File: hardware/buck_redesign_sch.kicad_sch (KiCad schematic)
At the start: 25 parts, among them Q7 MMBT3904, U101 L7987L, U5 TLV1701

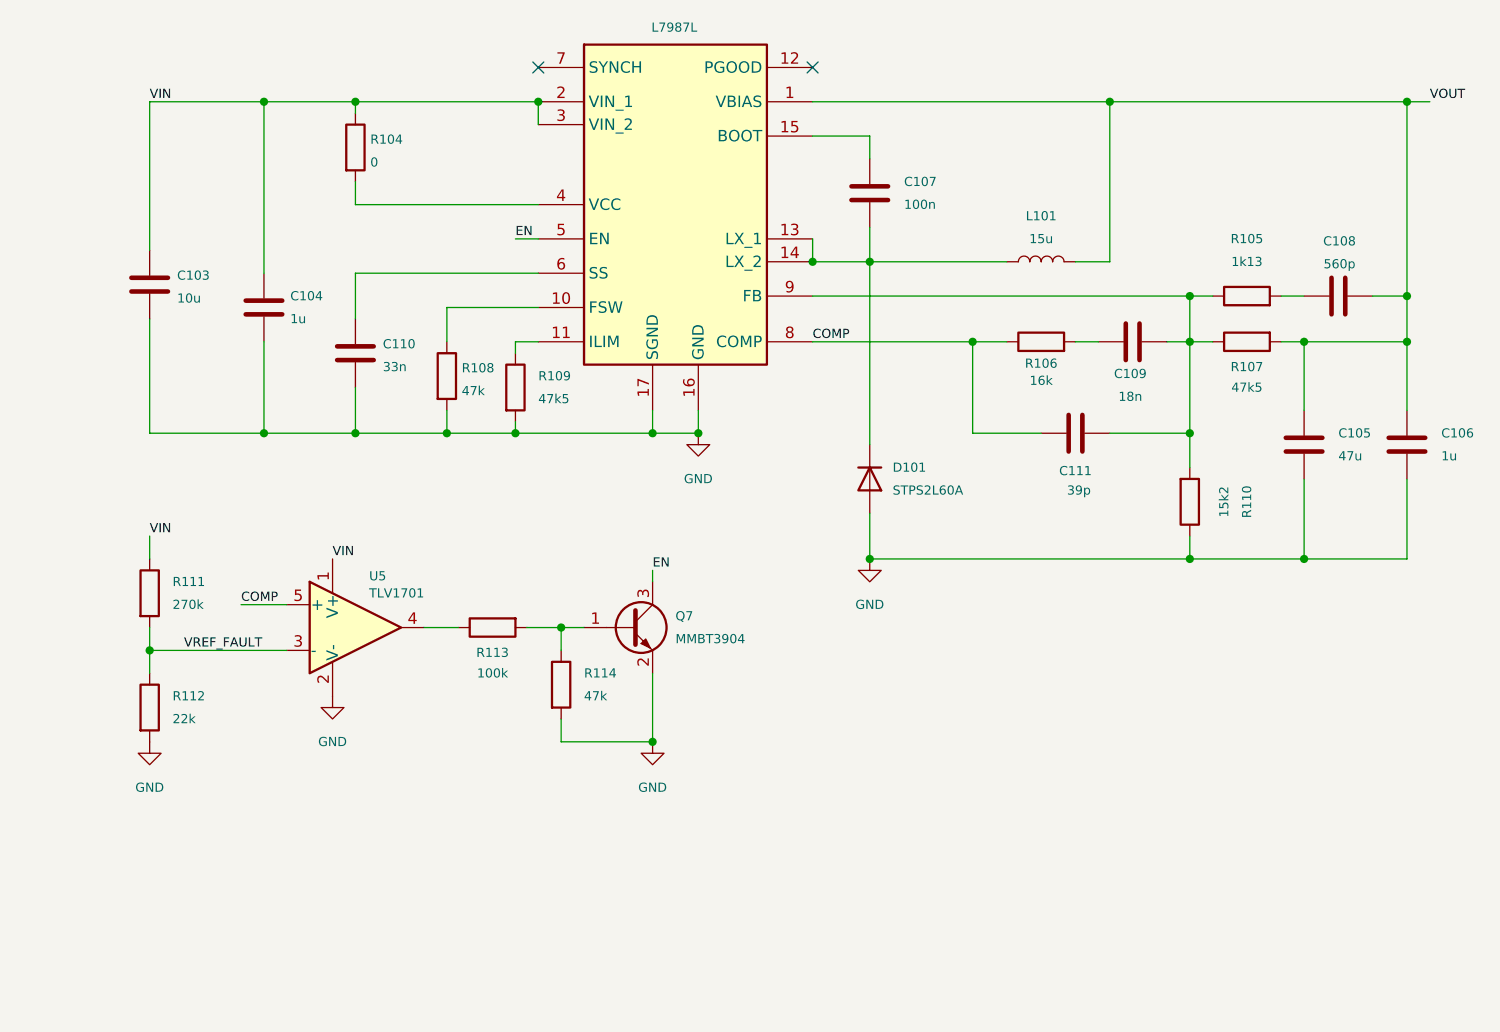
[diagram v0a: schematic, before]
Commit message: Corrected pins in TLV1701 symbol and added bypass cap on its V+
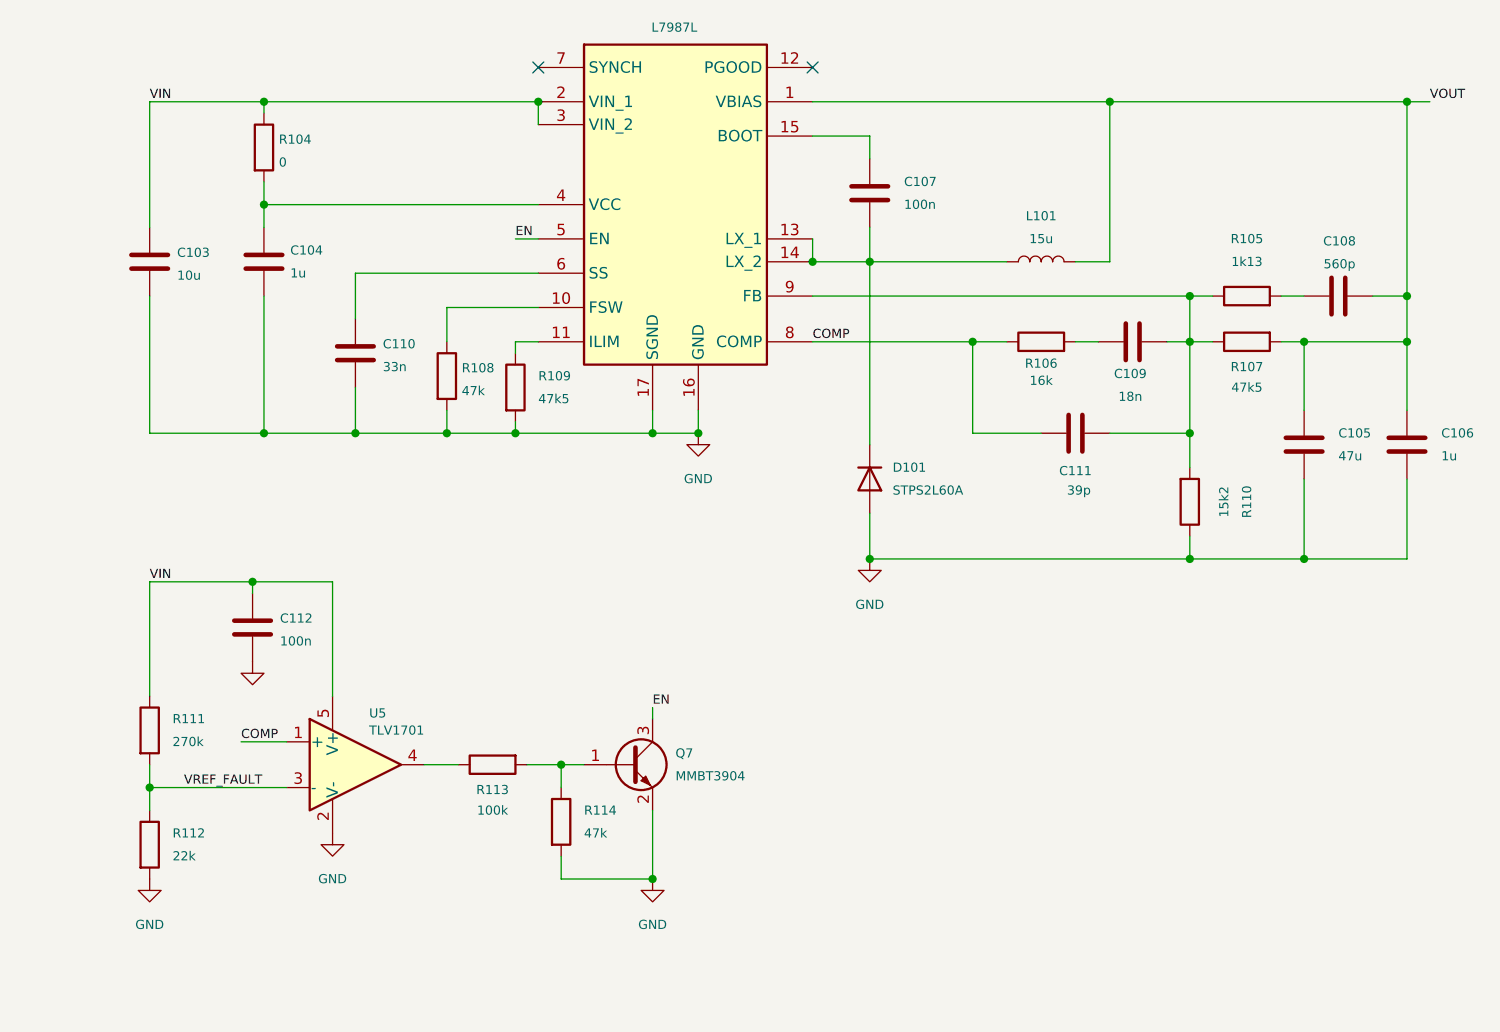
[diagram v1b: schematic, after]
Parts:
- added C112: 100n, symbol Device:C
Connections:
- net COMP: now also U5.1 (+); no longer U5.5 (+)
- net GND: now also C112.2
- net VIN: now also U5.5 (V+), C112.1; no longer C104.1, U5.1 (V+)
- net at R104.2, U101.4 (VCC): now also C104.1
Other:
- moved on the sheet: C103, C104, Q7, R104, R111, R112, R113, R114, U5

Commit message: Added components to comparator block
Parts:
- added C113: 330n, symbol Device:C
- added R115, R117: 100k, symbol Device:R
- added R116: 15k, symbol Device:R
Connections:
- net EN: now also C113.1, R115.2, R116.1
- net GND: now also C113.2, R116.2
- net VIN: now also R115.1, R117.1
- net at R113.1, U5.4: now also R117.2
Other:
- moved on the sheet: C112, Q7, R111, R112, R113, R114, U5

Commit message: Updated power schematic, delated buck schematic
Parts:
- C113: MPN EMK325BJ476MM-P, -> (none); Manufacturer Taiyo Yuden -> (none)
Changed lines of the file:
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@@
 			)
 		)
-		(property "MPN" "EMK325BJ476MM-P,"
+		(property "MPN" ""
 			(at 154.94 133.35 0)
 			(hide yes)
@@
 			)
 		)
-		(property "Manufacturer" "Taiyo Yuden"
+		(property "Manufacturer" ""
 			(at 154.94 133.35 0)
 			(hide yes)
